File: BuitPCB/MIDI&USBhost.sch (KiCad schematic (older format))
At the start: 10 parts

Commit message: Added most of components, few pending
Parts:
- C1: renamed from C?; footprint (none) -> Capacitor_SMD:C_0805_2012Metric
- J1, J2: renamed from J?; footprint (none) -> esp32s2:DJ005
- U2: renamed from U?; footprint (none) -> Package_DIP:DIP-8_W8.89mm_SMDSocket_LongPads
- gave numbers to parts that had none: 6
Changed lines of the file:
@@
 $EndDescr
 $Comp
-L Connector:DIN-5_180degree J?
+L Connector:DIN-5_180degree J1
 U 1 1 61AA292D
 P 4250 2500
-F 0 "J?" H 4250 2200 50  0000 C CNN
+F 0 "J1" H 4250 2200 50  0000 C CNN
 F 1 "DIN-5_180degree" H 4850 2350 50  0000 C CNN
-F 2 "" H 4250 2500 50  0001 C CNN
+F 2 "esp32s2:DJ005" H 4250 2500 50  0001 C CNN
 F 3 "http://www.mouser.com/ds/2/18/40_c091_abd_e-75918.pdf" H 4250 2500 50  0001 C CNN
 	1    4250 2500
@@
 $EndComp
 $Comp
-L Connector:DIN-5_180degree J?
+L Connector:DIN-5_180degree J2
 U 1 1 61AA3295
 P 5600 4350
-F 0 "J?" H 5600 4050 50  0000 C CNN
+F 0 "J2" H 5600 4050 50  0000 C CNN
 F 1 "DIN-5_180degree" H 6150 4200 50  0000 C CNN
-F 2 "" H 5600 4350 50  0001 C CNN
+F 2 "esp32s2:DJ005" H 5600 4350 50  0001 C CNN
 F 3 "http://www.mouser.com/ds/2/18/40_c091_abd_e-75918.pdf" H 5600 4350 50  0001 C CNN
 	1    5600 4350
@@
 $EndComp
 $Comp
-L Isolator:6N138 U?
+L Isolator:6N138 U2
 U 1 1 61B11288
 P 6100 2700
-F 0 "U?" H 6100 3167 50  0000 C CNN
+F 0 "U2" H 6100 3167 50  0000 C CNN
 F 1 "6N138" H 6100 3076 50  0000 C CNN
-F 2 "" H 6390 2400 50  0001 C CNN
+F 2 "Package_DIP:DIP-8_W8.89mm_SMDSocket_LongPads" H 6390 2400 50  0001 C CNN
 F 3 "http://www.onsemi.com/pub/Collateral/HCPL2731-D.pdf" H 6390 2400 50  0001 C CNN
 	1    6100 2700
@@
 $EndComp
 $Comp
-L Diode:CD4148W D?
+L Diode:CD4148W D1
 U 1 1 61B11F8F
 P 5100 2750
-F 0 "D?" V 5054 2830 50  0000 L CNN
+F 0 "D1" V 5054 2830 50  0000 L CNN
 F 1 "CD4148W" V 5145 2830 50  0000 L CNN
 F 2 "Diode_SMD:D_0805_2012Metric" H 5100 2550 50  0001 C CNN
@@
 $EndComp
 $Comp
-L Device:R R?
+L Device:R R1
 U 1 1 61B14D55
 P 4900 2600
-F 0 "R?" V 4693 2600 50  0000 C CNN
+F 0 "R1" V 4693 2600 50  0000 C CNN
 F 1 "220R" V 4784 2600 50  0000 C CNN
 F 2 "Resistor_SMD:R_0805_2012Metric" V 4830 2600 50  0001 C CNN
@@
 	5800 2900 5800 2800
 $Comp
-L Device:C C?
+L Device:C C1
 U 1 1 61B1910B
 P 6650 2750
-F 0 "C?" H 6765 2796 50  0000 L CNN
+F 0 "C1" H 6765 2796 50  0000 L CNN
 F 1 "C" H 6765 2705 50  0000 L CNN
-F 2 "" H 6688 2600 50  0001 C CNN
+F 2 "Capacitor_SMD:C_0805_2012Metric" H 6688 2600 50  0001 C CNN
 F 3 "~" H 6650 2750 50  0001 C CNN
 	1    6650 2750
@@
 $EndComp
 $Comp
-L Device:R R?
+L Device:R R4
 U 1 1 61B197C6
 P 7050 2550
-F 0 "R?" V 6843 2550 50  0000 C CNN
+F 0 "R4" V 6843 2550 50  0000 C CNN
 F 1 "470R" V 6934 2550 50  0000 C CNN
 F 2 "Resistor_SMD:R_0805_2012Metric" V 6980 2550 50  0001 C CNN
@@
 	6400 2900 6650 2900
 $Comp
-L power:+5V #PWR?
+L power:+5V #PWR01
 U 1 1 61B1B539
 P 6650 2500
-F 0 "#PWR?" H 6650 2350 50  0001 C CNN
+F 0 "#PWR01" H 6650 2350 50  0001 C CNN
 F 1 "+5V" H 6665 2673 50  0000 C CNN
 F 2 "" H 6650 2500 50  0001 C CNN
@@
 Connection ~ 6650 2500
 $Comp
-L power:GND #PWR?
+L power:GND #PWR02
 U 1 1 61B1C43B
 P 6650 2900
-F 0 "#PWR?" H 6650 2650 50  0001 C CNN
+F 0 "#PWR02" H 6650 2650 50  0001 C CNN
 F 1 "GND" H 6655 2727 50  0000 C CNN
 F 2 "" H 6650 2900 50  0001 C CNN
@@
 Connection ~ 6650 2900
 $Comp
-L power:+3V3 #PWR?
+L power:+3V3 #PWR04
 U 1 1 61B1C9AF
 P 7200 2400
-F 0 "#PWR?" H 7200 2250 50  0001 C CNN
+F 0 "#PWR04" H 7200 2250 50  0001 C CNN
 F 1 "+3V3" H 7215 2573 50  0000 C CNN
 F 2 "" H 7200 2400 50  0001 C CNN
@@
 Connection ~ 5100 2900
 $Comp
-L Device:R R?
+L Device:R R2
 U 1 1 61B2373F
 P 6350 4450
-F 0 "R?" V 6143 4450 50  0000 C CNN
+F 0 "R2" V 6143 4450 50  0000 C CNN
 F 1 "47R" V 6234 4450 50  0000 C CNN
 F 2 "Resistor_SMD:R_0805_2012Metric" V 6280 4450 50  0001 C CNN
@@
 $EndComp
 $Comp
-L Device:R R?
+L Device:R R3
 U 1 1 61B240B9
 P 6350 4800
-F 0 "R?" V 6143 4800 50  0000 C CNN
+F 0 "R3" V 6143 4800 50  0000 C CNN
 F 1 "47R" V 6234 4800 50  0000 C CNN
 F 2 "Resistor_SMD:R_0805_2012Metric" V 6280 4800 50  0001 C CNN
@@
 	6200 4450 5900 4450
 $Comp
-L power:+3V3 #PWR?
+L power:+3V3 #PWR03
 U 1 1 61B2580F
 P 6700 4400
-F 0 "#PWR?" H 6700 4250 50  0001 C CNN
+F 0 "#PWR03" H 6700 4250 50  0001 C CNN
 F 1 "+3V3" H 6715 4573 50  0000 C CNN
 F 2 "" H 6700 4400 50  0001 C CNN
@@
 AR Path="/61B32646" Ref="J?"  Part="1"
 AR Path="/61A97DFC/61B32646" Ref="J?"  Part="1"
-F 0 "J?" H 9057 4167 50  0000 C CNN
+AR Path="/61AA26AB/61B32646" Ref="J3"  Part="1"
+F 0 "J3" H 9057 4167 50  0000 C CNN
 F 1 "USB_A" H 9057 4076 50  0000 C CNN
 F 2 "Connector_USB:USB_A_Stewart_SS-52100-001_Horizontal" H 9150 3650 50  0001 C CNN
@@
 U 1 1 61B3264C
 P 9000 4100
-F 0 "#PWR?" H 9000 3850 50  0001 C CNN
+AR Path="/61A97DFC/61B3264C" Ref="#PWR?"  Part="1"
+AR Path="/61AA26AB/61B3264C" Ref="#PWR05"  Part="1"
+F 0 "#PWR05" H 9000 3850 50  0001 C CNN
 F 1 "GND" H 9005 3927 50  0000 C CNN
 F 2 "" H 9000 4100 50  0001 C CNN

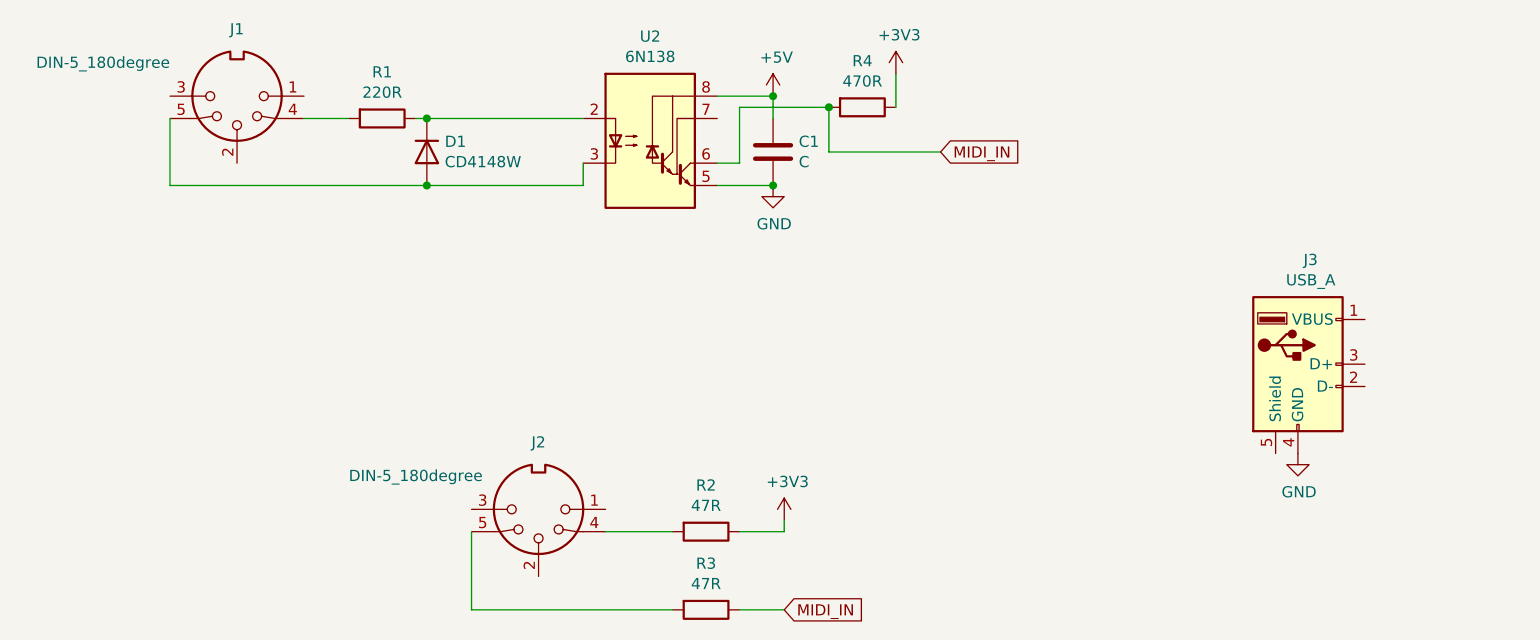
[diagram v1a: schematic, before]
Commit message: Added sensors connectors
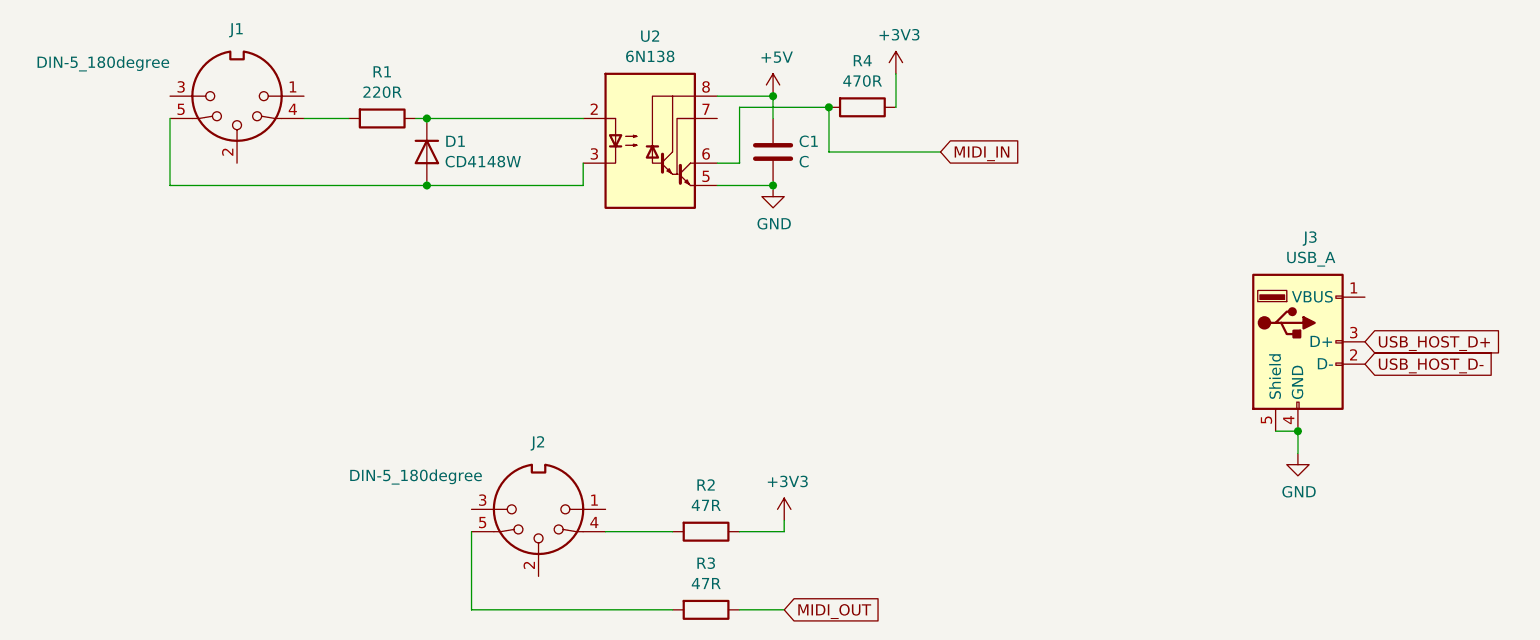
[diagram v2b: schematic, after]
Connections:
- net GND: now also J3.5 (Shield)
- net MIDI_IN: no longer R3.1
- net USB_HOST_D-: now reaches J3.2 (D-)
- net USB_HOST_D+: now reaches J3.3 (D+)
- new net MIDI_OUT: R3.1
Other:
- moved on the sheet: J3
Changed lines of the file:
@@
 $Descr A4 11693 8268
 encoding utf-8
-Sheet 3 5
+Sheet 3 6
 Title ""
 Date ""
@@
 $EndComp
 Text GLabel 6700 4800 2    50   Input ~ 0
-MIDI_IN
+MIDI_OUT
 Wire Wire Line
 	6700 4400 6700 4450
@@
 L Connector:USB_A J?
 U 1 1 61B32646
-P 9000 3700
+P 9000 3600
 AR Path="/61B32646" Ref="J?"  Part="1"
 AR Path="/61A97DFC/61B32646" Ref="J?"  Part="1"
 AR Path="/61AA26AB/61B32646" Ref="J3"  Part="1"
-F 0 "J3" H 9057 4167 50  0000 C CNN
-F 1 "USB_A" H 9057 4076 50  0000 C CNN
-F 2 "Connector_USB:USB_A_Stewart_SS-52100-001_Horizontal" H 9150 3650 50  0001 C CNN
-F 3 " ~" H 9150 3650 50  0001 C CNN
-	1    9000 3700
+F 0 "J3" H 9057 4067 50  0000 C CNN
+F 1 "USB_A" H 9057 3976 50  0000 C CNN
+F 2 "Connector_USB:USB_A_Stewart_SS-52100-001_Horizontal" H 9150 3550 50  0001 C CNN
+F 3 " ~" H 9150 3550 50  0001 C CNN
+	1    9000 3600
 	1    0    0    -1
 $EndComp
@@
 	1    0    0    -1
 $EndComp
+Wire Wire Line
+	8900 4000 9000 4000
+Wire Wire Line
+	9000 4000 9000 4100
+Connection ~ 9000 4000
+Text GLabel 9300 3600 2    50   Input ~ 0
+USB_HOST_D+
+Text GLabel 9300 3700 2    50   Input ~ 0
+USB_HOST_D-
 $EndSCHEMATC

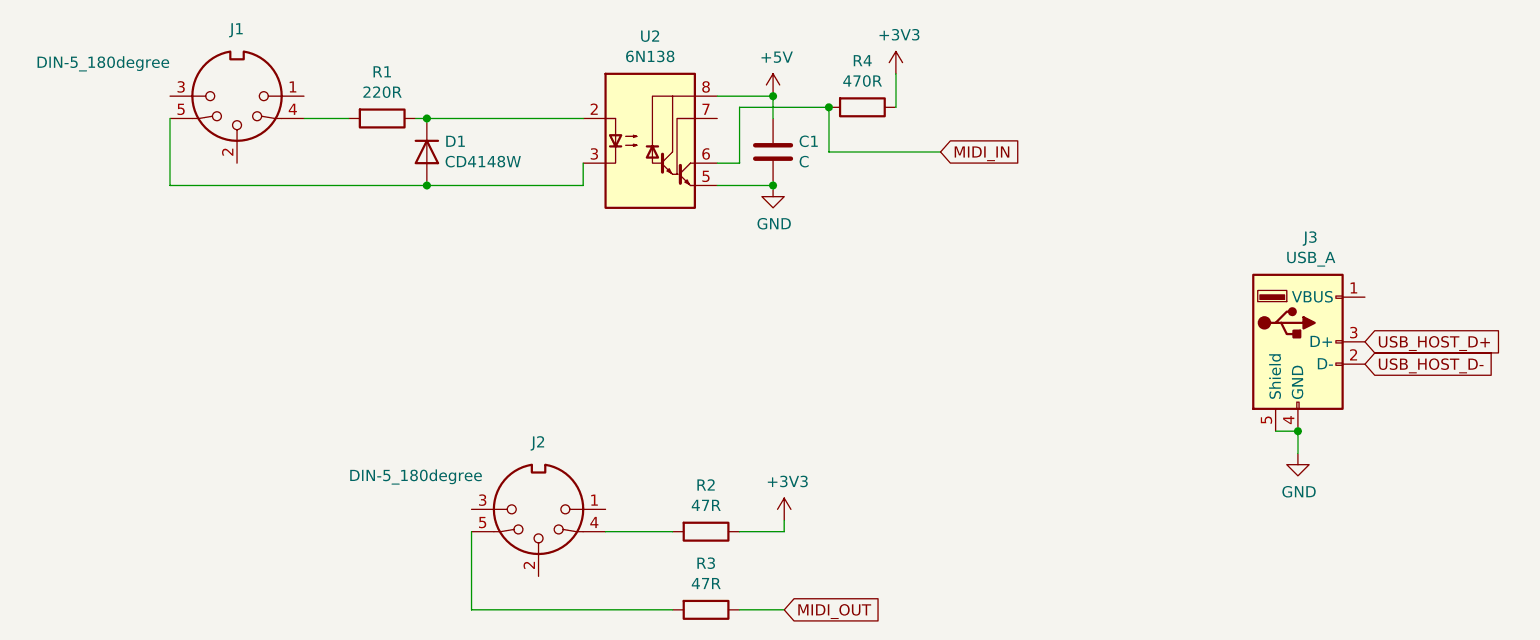
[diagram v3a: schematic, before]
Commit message: Updated to almost every component and started routing
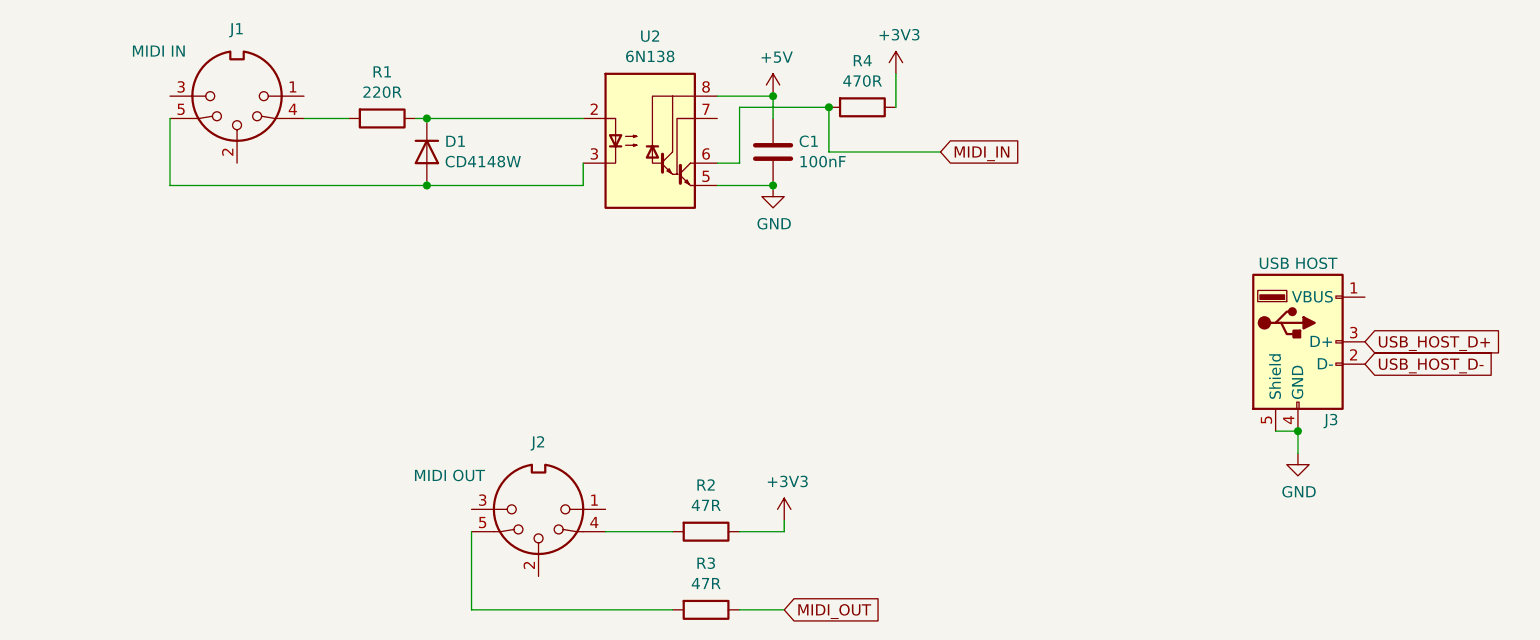
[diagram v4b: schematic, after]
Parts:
- C1: value C -> 100nF
- J1: value DIN-5_180degree -> MIDI IN
- J2: value DIN-5_180degree -> MIDI OUT
- J3: value USB_A -> USB HOST
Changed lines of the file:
@@
 P 4250 2500
 F 0 "J1" H 4250 2200 50  0000 C CNN
-F 1 "DIN-5_180degree" H 4850 2350 50  0000 C CNN
+F 1 "MIDI IN" H 4600 2300 50  0000 C CNN
 F 2 "esp32s2:DJ005" H 4250 2500 50  0001 C CNN
 F 3 "http://www.mouser.com/ds/2/18/40_c091_abd_e-75918.pdf" H 4250 2500 50  0001 C CNN
@@
 P 5600 4350
 F 0 "J2" H 5600 4050 50  0000 C CNN
-F 1 "DIN-5_180degree" H 6150 4200 50  0000 C CNN
+F 1 "MIDI OUT" H 6000 4200 50  0000 C CNN
 F 2 "esp32s2:DJ005" H 5600 4350 50  0001 C CNN
 F 3 "http://www.mouser.com/ds/2/18/40_c091_abd_e-75918.pdf" H 5600 4350 50  0001 C CNN
@@
 P 6650 2750
 F 0 "C1" H 6765 2796 50  0000 L CNN
-F 1 "C" H 6765 2705 50  0000 L CNN
+F 1 "100nF" H 6765 2705 50  0000 L CNN
 F 2 "Capacitor_SMD:C_0805_2012Metric" H 6688 2600 50  0001 C CNN
 F 3 "~" H 6650 2750 50  0001 C CNN
@@
 AR Path="/61A97DFC/61B32646" Ref="J?"  Part="1"
 AR Path="/61AA26AB/61B32646" Ref="J3"  Part="1"
-F 0 "J3" H 9057 4067 50  0000 C CNN
-F 1 "USB_A" H 9057 3976 50  0000 C CNN
+F 0 "J3" H 9150 3250 50  0000 C CNN
+F 1 "USB HOST" H 9000 3950 50  0000 C CNN
 F 2 "Connector_USB:USB_A_Stewart_SS-52100-001_Horizontal" H 9150 3550 50  0001 C CNN
 F 3 " ~" H 9150 3550 50  0001 C CNN
